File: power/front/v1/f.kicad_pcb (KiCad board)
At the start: 2 copper layers, 20.3 x 102.9 mm, 7 parts, among them J1 fm_power_i, J10 input

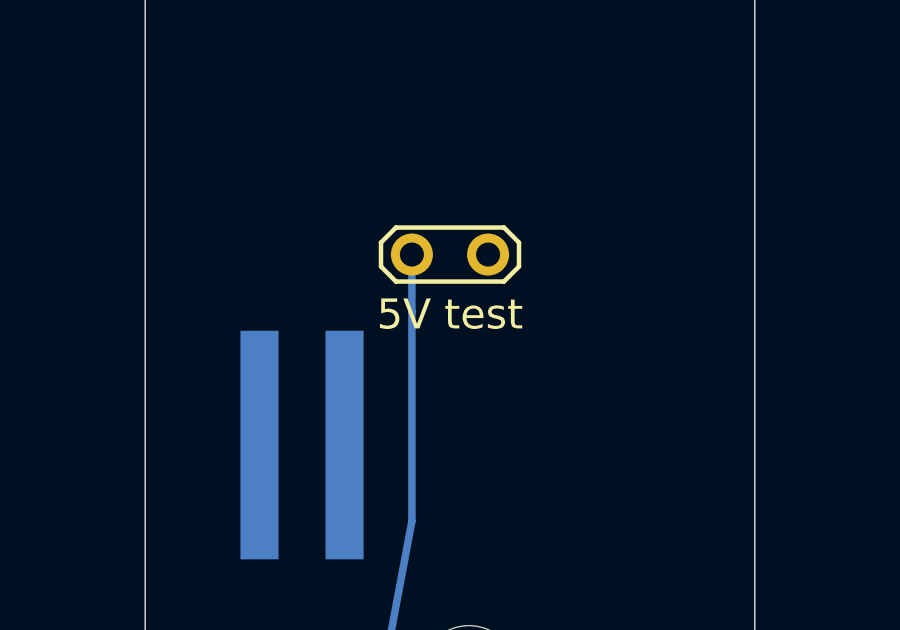
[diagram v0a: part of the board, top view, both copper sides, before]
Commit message: voltage regulator for each module
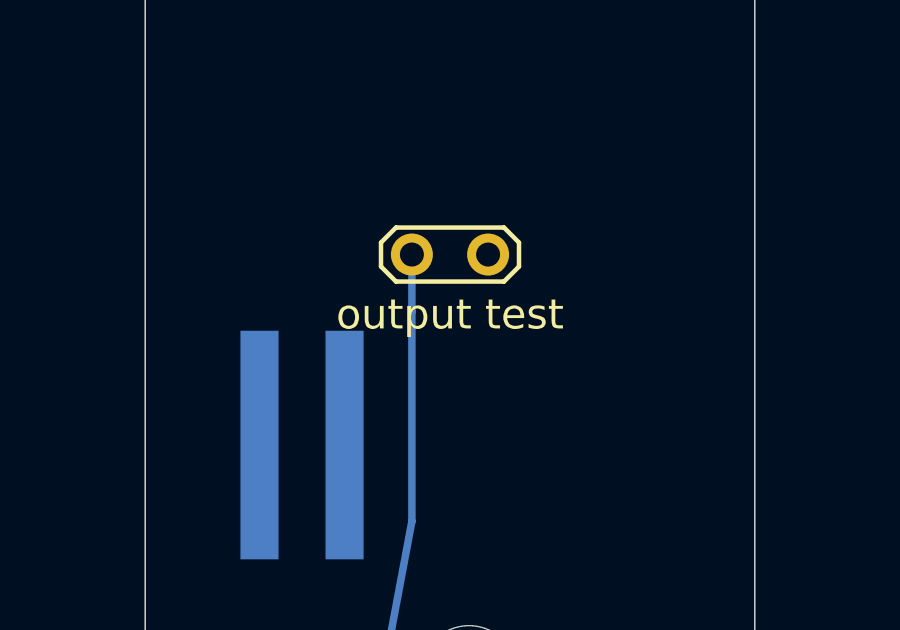
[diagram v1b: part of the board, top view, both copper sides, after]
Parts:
- TP1: value 5V test -> output test
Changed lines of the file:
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@@
       (effects (font (size 1 1) (thickness 0.15)))
     )
-    (fp_text value "5V test" (at 1.27 2) (layer F.SilkS)
+    (fp_text value "output test" (at 1.27 2) (layer F.SilkS)
       (effects (font (size 1 1) (thickness 0.15)))
     )
